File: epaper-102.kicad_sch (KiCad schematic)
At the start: 20 parts, among them J1 Conn_01x30_Female, J2 connector

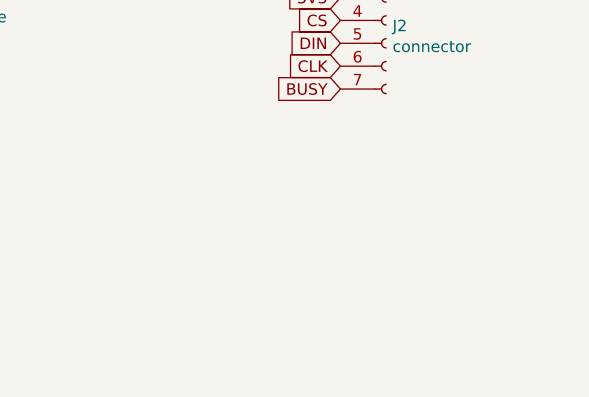
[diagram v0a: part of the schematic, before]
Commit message: add two mounting socket and optimize the the dimensions
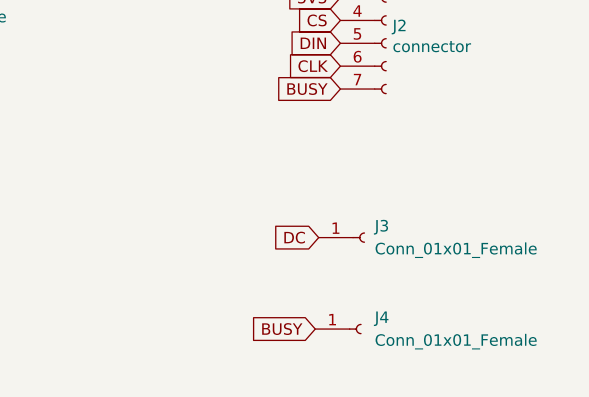
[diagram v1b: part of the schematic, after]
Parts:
- added J3, J4: Conn_01x01_Female, Connector_PinHeader_2.54mm:PinHeader_1x01_P2.54mm_Vertical, symbol Connector:Conn_01x01_Female
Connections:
- net BUSY: now also J4.1 (Pin_1)
- net DC: now also J3.1 (Pin_1)
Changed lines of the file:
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@@
+    )
+  )
+  (global_label "BUSY" (shape input) (at 107.696 90.805 180) (fields_autoplaced)
+    (effects (font (size 1.27 1.27)) (justify right))
+    (property "Intersheet References" "${INTERSHEET_REFS}" (id 0) (at 100.4732 90.7256 0)
+      (effects (font (size 1.27 1.27)) (justify right) hide)
     )
   )
@@
     (property "Intersheet References" "${INTERSHEET_REFS}" (id 0) (at 0 0 0)
       (effects (font (size 1.27 1.27)) hide)
+    )
+  )
+  (global_label "DC" (shape input) (at 108.077 80.645 180) (fields_autoplaced)
+    (effects (font (size 1.27 1.27)) (justify right))
+    (property "Intersheet References" "${INTERSHEET_REFS}" (id 0) (at 103.2128 80.5656 0)
+      (effects (font (size 1.27 1.27)) (justify right) hide)
     )
   )
@@
     (pin "2")
   )
+  (symbol (lib_id "Connector:Conn_01x01_Female") (at 113.157 80.645 0) (unit 1)
+    (in_bom yes) (on_board yes) (fields_autoplaced)
+    (property "Reference" "J3" (id 0) (at 114.3 79.3749 0)
+      (effects (font (size 1.27 1.27)) (justify left))
+    )
+    (property "Value" "Conn_01x01_Female" (id 1) (at 114.3 81.9149 0)
+      (effects (font (size 1.27 1.27)) (justify left))
+    )
+    (property "Footprint" "Connector_PinHeader_2.54mm:PinHeader_1x01_P2.54mm_Vertical" (id 2) (at 113.157 80.645 0)
+      (effects (font (size 1.27 1.27)) hide)
+    )
+    (property "Datasheet" "~" (id 3) (at 113.157 80.645 0)
+      (effects (font (size 1.27 1.27)) hide)
+    )
+    (pin "1")
+  )
+  (symbol (lib_id "Connector:Conn_01x01_Female") (at 112.776 90.805 0) (unit 1)
+    (in_bom yes) (on_board yes) (fields_autoplaced)
+    (property "Reference" "J4" (id 0) (at 114.3 89.5349 0)
+      (effects (font (size 1.27 1.27)) (justify left))
+    )
+    (property "Value" "Conn_01x01_Female" (id 1) (at 114.3 92.0749 0)
+      (effects (font (size 1.27 1.27)) (justify left))
+    )
+    (property "Footprint" "Connector_PinHeader_2.54mm:PinHeader_1x01_P2.54mm_Vertical" (id 2) (at 112.776 90.805 0)
+      (effects (font (size 1.27 1.27)) hide)
+    )
+    (property "Datasheet" "~" (id 3) (at 112.776 90.805 0)
+      (effects (font (size 1.27 1.27)) hide)
+    )
+    (pin "1")
+  )
   (sheet_instances
     (path "/" (page "1"))
@@
       (reference "J2") (unit 1) (value "connector") (footprint "Connector_PinHeader_2.54mm:PinHeader_1x07_P2.54mm_Vertical")
     )
-  )
+    (path "/7fa098fb-b644-4e64-920e-8328b5d12f21"
+      (reference "J3") (unit 1) (value "Conn_01x01_Female") (footprint "Connector_PinHeader_2.54mm:PinHeader_1x01_P2.54mm_Vertical")
+    )
+    (path "/d93d269d-5381-4718-9ad0-eea6c95f2fda"
+      (reference "J4") (unit 1) (value "Conn_01x01_Female") (footprint "Connector_PinHeader_2.54mm:PinHeader_1x01_P2.54mm_Vertical")
+    )
+  )
